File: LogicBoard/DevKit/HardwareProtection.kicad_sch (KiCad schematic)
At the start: 23 parts, among them U11 SN74LVC1G332DCKR, U15 TPL0401B-10DCKR, U16 ATTINY1616-MNR, U17 ATTINY1616-MNR, U2 TPL0401A-10DCKR

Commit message: v2
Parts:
- removed D3: SS14, Diode_SMD:D_SMA, symbol Device:D_Schottky
- removed U2: TPL0401A-10DCKR, Package_TO_SOT_SMD:Texas_R-PDSO-G6, symbol Potentiometer_Digital:TPL0401A-10-Q1
- added D8: 1N5819WS, Diode_SMD:D_SOD-323, symbol Device:D_Schottky
- added D9 (x3): L_FAULT, LED_SMD:LED_0603_1608Metric, symbol Device:LED
- added J4: HWProtDebug, Connector_PinHeader_2.00mm:PinHeader_1x04_P2.00mm_Vertical, symbol Connector_Generic:Conn_01x04
- added R1 (x4): 4.7k, Resistor_SMD:R_0603_1608Metric, symbol Device:R
- added R47 (x3): 10k, Resistor_SMD:R_0603_1608Metric, symbol Device:R
- added U2: TPL0401B-10DCKR, Package_TO_SOT_SMD:Texas_R-PDSO-G6, symbol Potentiometer_Digital:TPL0401B-10-Q1
- C15: footprint Capacitor_SMD:C_0805_2012Metric -> Capacitor_SMD:C_0603_1608Metric; MPN (none) -> C14663
- C23, C24: MPN (none) -> C107145
- C5, C6: footprint Capacitor_SMD:C_0805_2012Metric -> Capacitor_SMD:C_0603_1608Metric; MPN (none) -> C15849
- R15: footprint Resistor_SMD:R_0805_2012Metric -> Resistor_SMD:R_0603_1608Metric; MPN C17414 -> C25804
- R33: footprint Resistor_SMD:R_0805_2012Metric -> Resistor_SMD:R_0603_1608Metric; MPN (none) -> C25804
- R43, R44, R45: footprint Resistor_SMD:R_0805_2012Metric -> Resistor_SMD:R_0603_1608Metric; MPN (none) -> C4190
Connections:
- net +3.3V: now also R1.1, R1.1, R1.1, R1.1, U2.1 (VDD)
- net +3.3VADC: now also U2.6 (H)
- net CURR_TRIP_HIGH: now also U2.5 (W)
- net GND: now also R47.2, R47.2, R47.2, U2.2 (GND)
- net POWER_STAGE_DISABLE: now also D9.2 (A)
- net POWER_STAGE_LOCKOUT: now also D8.1 (K)
- net AT_HIGH_FAULT: now reaches R33.2, U11.6, U16.5 (PA4)
- net AT_HIGH_FAULT: now also D9.2 (A)
- net at U11.4: now also D8.2 (A)
- net AT_LOW_FAULT: now reaches R33.2, U11.1, U17.5 (PA4)
- net AT_LOW_FAULT: now also D9.2 (A)
- net AT_HIGH_RX: now reaches U16.11 (PB3)
- net AT_HIGH_RX: now also J4.3 (Pin_3)
- net AT_HIGH_TX: now reaches U16.12 (PB2)
- net AT_HIGH_TX: now also J4.4 (Pin_4)
- net AT_LOW_SCL: now reaches U17.1 (PA2)
- net AT_LOW_SCL: now also U15.3 (SCL), R1.2
- net AT_LOW_RX: now reaches U17.11 (PB3)
- net AT_LOW_RX: now also J4.1 (Pin_1)
- net AT_LOW_TX: now reaches U17.12 (PB2)
- net AT_LOW_TX: now also J4.2 (Pin_2)
- net AT_LOW_SDA: now reaches U17.20 (PA1)
- net AT_LOW_SDA: now also U15.4 (SDA), R1.2
- net SCL renamed AT_HIGH_SCL
- net AT_HIGH_SCL: now also R1.2, U2.3 (SCL); no longer U15.3 (SCL)
- net SDA renamed AT_HIGH_SDA
- net AT_HIGH_SDA: now also R1.2, U2.4 (SDA); no longer U15.4 (SDA)
- new net: D9.1 (K), R47.1 (x3)
- no-connect marks 18 -> 12
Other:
- note added: "use TPL0401A-10DCKR if B is not available B is cheaper"
- moved on the sheet: C5, C53, C54, C6, R15, U15

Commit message: v2
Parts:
- added TP3: HighTrip, TestPoint:TestPoint_Pad_D1.0mm, symbol Connector:TestPoint
- added TP3: LowTrip, TestPoint:TestPoint_Pad_D1.0mm, symbol Connector:TestPoint
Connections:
- net CLEAR_HW_FAULT: now also U16.9 (PB5), U17.9 (PB5)
- net CURR_TRIP_HIGH: now also TP3.1
- net CURR_TRIP_LOW: now also TP3.1
- no-connect marks 12 -> 10
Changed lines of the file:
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@@
   )
   (no_connect (at 130.81 72.39))
-  (no_connect (at 130.81 100.33))
   (no_connect (at 100.33 172.72))
-  (no_connect (at 130.81 177.8))
   (no_connect (at 100.33 87.63))
   (no_connect (at 100.33 92.71))
@@
     (stroke (width 0) (type default))
   )
-  (wire (pts (xy 67.31 82.55) (xy 54.61 82.55))
+  (wire (pts (xy 64.77 82.55) (xy 54.61 82.55))
     (stroke (width 0) (type default))
   )
@@
     (stroke (width 0) (type default))
   )
-  (wire (pts (xy 67.31 73.66) (xy 67.31 82.55))
+  (wire (pts (xy 64.77 73.66) (xy 64.77 82.55))
     (stroke (width 0) (type default))
   )
@@
     )
   )
+  (global_label "CLEAR_HW_FAULT" (shape input) (at 130.81 100.33 0) (fields_autoplaced)
+    (effects (font (size 1.27 1.27)) (justify left))
+    (property "Intersheetrefs" "${INTERSHEET_REFS}" (at 149.0878 100.33 0)
+      (effects (font (size 1.27 1.27)) (justify left) hide)
+    )
+  )
   (global_label "POWER_STAGE_DISABLE" (shape input) (at 194.31 151.13 180) (fields_autoplaced)
     (effects (font (size 1.27 1.27)) (justify right))
@@
     (effects (font (size 1.27 1.27)) (justify left))
     (property "Intersheetrefs" "${INTERSHEET_REFS}" (at 149.4397 82.55 0)
+      (effects (font (size 1.27 1.27)) (justify left) hide)
+    )
+  )
+  (global_label "CLEAR_HW_FAULT" (shape input) (at 130.81 177.8 0) (fields_autoplaced)
+    (effects (font (size 1.27 1.27)) (justify left))
+    (property "Intersheetrefs" "${INTERSHEET_REFS}" (at 149.0878 177.8 0)
       (effects (font (size 1.27 1.27)) (justify left) hide)
     )
@@
     )
   )
-  (symbol (lib_id "power:+3.3VADC") (at 67.31 73.66 0) (unit 1)
-    (in_bom yes) (on_board yes) (dnp no) (fields_autoplaced)
-    (property "Reference" "#PWR0127" (at 71.12 74.93 0)
-      (effects (font (size 1.27 1.27)) hide)
-    )
-    (property "Value" "+3.3VADC" (at 67.31 68.58 0)
-      (effects (font (size 1.27 1.27)))
-    )
-    (property "Footprint" "" (at 67.31 73.66 0)
-      (effects (font (size 1.27 1.27)) hide)
-    )
-    (property "Datasheet" "" (at 67.31 73.66 0)
+  (symbol (lib_id "power:+3.3VADC") (at 64.77 73.66 0) (unit 1)
+    (in_bom yes) (on_board yes) (dnp no) (fields_autoplaced)
+    (property "Reference" "#PWR0127" (at 68.58 74.93 0)
+      (effects (font (size 1.27 1.27)) hide)
+    )
+    (property "Value" "+3.3VADC" (at 64.77 68.58 0)
+      (effects (font (size 1.27 1.27)))
+    )
+    (property "Footprint" "" (at 64.77 73.66 0)
+      (effects (font (size 1.27 1.27)) hide)
+    )
+    (property "Datasheet" "" (at 64.77 73.66 0)
       (effects (font (size 1.27 1.27)) hide)
     )
@@
     )
   )
+  (symbol (lib_id "Connector:TestPoint") (at 69.85 90.17 0) (unit 1)
+    (in_bom yes) (on_board yes) (dnp no)
+    (property "Reference" "TP3" (at 68.58 81.28 0)
+      (effects (font (size 1.27 1.27)) (justify left))
+    )
+    (property "Value" "HighTrip" (at 66.04 83.82 0)
+      (effects (font (size 1.27 1.27)) (justify left))
+    )
+    (property "Footprint" "TestPoint:TestPoint_Pad_D1.0mm" (at 74.93 90.17 0)
+      (effects (font (size 1.27 1.27)) hide)
+    )
+    (property "Datasheet" "~" (at 74.93 90.17 0)
+      (effects (font (size 1.27 1.27)) hide)
+    )
+    (pin "1")
+    (instances
+      (project "DevKit"
+        (path "/768a484b-8a27-40cf-8cad-0f63935b1af0"
+          (reference "TP3") (unit 1)
+        )
+        (path "/768a484b-8a27-40cf-8cad-0f63935b1af0/81081265-f675-4f9d-bffe-8ec1eaaaba23"
+          (reference "TP3") (unit 1)
+        )
+      )
+    )
+  )
   (symbol (lib_id "Device:R") (at 200.66 34.29 0) (unit 1)
     (in_bom yes) (on_board yes) (dnp no) (fields_autoplaced)
@@
         )
       )
+    )
+  )
+  (symbol (lib_id "Connector:TestPoint") (at 71.12 161.29 0) (unit 1)
+    (in_bom yes) (on_board yes) (dnp no)
+    (property "Reference" "TP3" (at 69.85 152.4 0)
+      (effects (font (size 1.27 1.27)) (justify left))
+    )
+    (property "Value" "LowTrip" (at 67.31 154.94 0)
+      (effects (font (size 1.27 1.27)) (justify left))
+    )
+    (property "Footprint" "TestPoint:TestPoint_Pad_D1.0mm" (at 76.2 161.29 0)
+      (effects (font (size 1.27 1.27)) hide)
+    )
+    (property "Datasheet" "~" (at 76.2 161.29 0)
+      (effects (font (size 1.27 1.27)) hide)
+    )
+    (pin "1")
+    (instances
+      (project "DevKit"
+        (path "/768a484b-8a27-40cf-8cad-0f63935b1af0"
+          (reference "TP3") (unit 1)
+        )
+        (path "/768a484b-8a27-40cf-8cad-0f63935b1af0/81081265-f675-4f9d-bffe-8ec1eaaaba23"
+          (reference "TP4") (unit 1)
+        )
+      )

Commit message: initialv2
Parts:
- removed C5, C6: 1u, Capacitor_SMD:C_0603_1608Metric, symbol Device:C
- removed C53, C54, C55, C56: 1u, Capacitor_SMD:C_0402_1005Metric, symbol Device:C
- removed D9 (x2): L_FAULT, LED_SMD:LED_0603_1608Metric, symbol Device:LED
- removed J4: HWProtDebug, Connector_PinHeader_2.00mm:PinHeader_1x04_P2.00mm_Vertical, symbol Connector_Generic:Conn_01x04
- removed R1 (x4): 4.7k, Resistor_SMD:R_0603_1608Metric, symbol Device:R
- removed R47 (x2): 10k, Resistor_SMD:R_0603_1608Metric, symbol Device:R
- removed TP3: HighTrip, TestPoint:TestPoint_Pad_D1.0mm, symbol Connector:TestPoint
- removed TP3: LowTrip, TestPoint:TestPoint_Pad_D1.0mm, symbol Connector:TestPoint
- removed U15, U2: TPL0401B-10DCKR, Package_TO_SOT_SMD:Texas_R-PDSO-G6, symbol Potentiometer_Digital:TPL0401B-10-Q1
- removed U16, U17: ATTINY1616-MNR, Package_DFN_QFN:VQFN-20-1EP_3x3mm_P0.4mm_EP1.7x1.7mm, symbol MCU_Microchip_ATtiny:ATtiny1616-M
- C22, C23, C24: value 220p 50v -> 220p; footprint Capacitor_SMD:C_0805_2012Metric -> Capacitor_SMD:C_0603_1608Metric; MPN C107145 -> C1603
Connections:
- net AT_HIGH_FAULT renamed ComparatorHigh/LATCH_OUT
- net AT_LOW_FAULT renamed ComparatorLow/LATCH_OUT
- no-connect marks 10 -> 0
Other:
- added sheet ComparatorHigh (ATTinyComp.kicad_sch)
- added sheet ComparatorLow (ATTinyComp.kicad_sch)
- note added: "330kHz Filters"
- note removed: "use TPL0401A-10DCKR if B is not available B is cheaper"
- moved on the sheet: D9, R15, R47

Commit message: v2
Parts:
- removed C22, C23, C24: 220p, Capacitor_SMD:C_0603_1608Metric, symbol Device:C
- removed R43, R44, R45: 2.2k, Resistor_SMD:R_0603_1608Metric, symbol Device:R
- C15: footprint Capacitor_SMD:C_0603_1608Metric -> GigaVescLibs:C_0603_1608Metric_L
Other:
- note removed: "330kHz Filters"
- moved on the sheet: D9, R15, R47

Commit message: small fixes
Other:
- note added: "If you do not want to use hardware protection, also remember to not solder R26 and R31"
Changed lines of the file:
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@@
+    (effects (font (size 1.27 1.27)) (justify left bottom))
+  )
+  (text "If you do not want to use hardware protection, also remember to not solder R26 and R31"
+    (at 72.39 35.56 0)
     (effects (font (size 1.27 1.27)) (justify left bottom))
   )

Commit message: v2.7.0 - Phase shunts
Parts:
- added C22, C23, C24: 1n, GigaVescLibs:C_0603_1608Metric_L, symbol Device:C
- added R43 (x3): 1k, Resistor_SMD:R_0603_1608Metric, symbol Device:R
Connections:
- net CURR1_FILTERED: now also C24.1, R43.1
- net CURR2_FILTERED: now also C23.1, R43.1
- net CURR3_FILTERED: now also C22.2, R43.1
- net GND: now also C22.1, C23.2, C24.2
- new net CURR1: R43.2
- new net CURR2: R43.2
- new net CURR3: R43.2

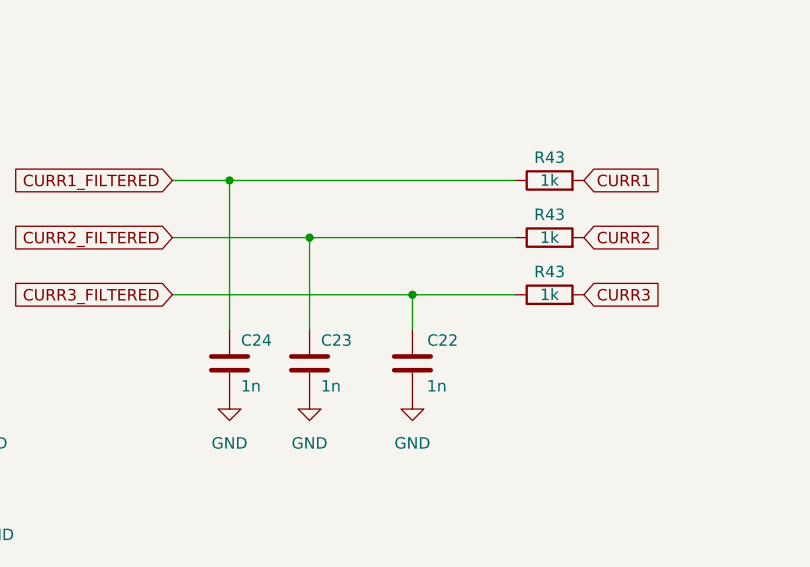
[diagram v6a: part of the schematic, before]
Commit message: v2.10.0 - Low side shunt and hall sensor - current filters
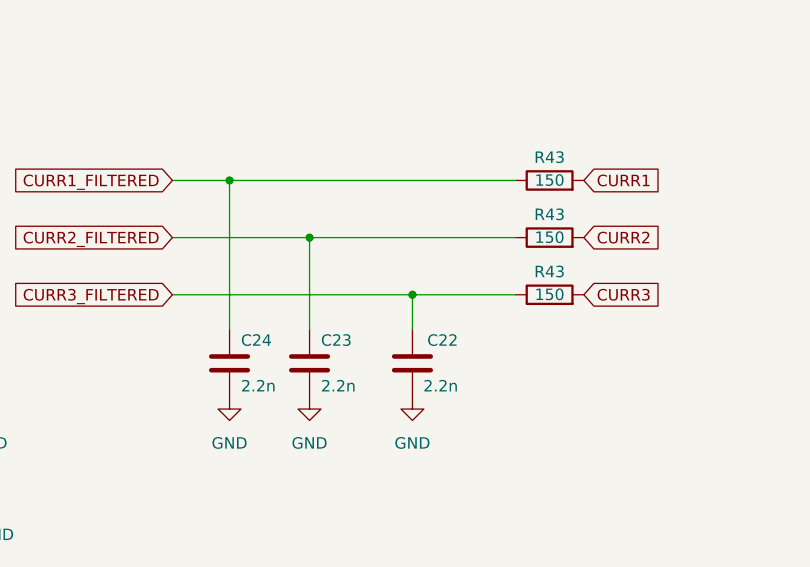
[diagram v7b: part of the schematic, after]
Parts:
- C22, C23, C24: value 1n -> 2.2n; MPN C1588 -> C1604
- R43: value 1k -> 150; MPN C21190 -> C22808
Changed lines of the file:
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@@
       (effects (font (size 1.27 1.27)))
     )
-    (property "Value" "1k" (at 229.87 93.98 90)
+    (property "Value" "150" (at 229.87 93.98 90)
       (effects (font (size 1.27 1.27)))
     )
@@
       (effects (font (size 1.27 1.27)) hide)
     )
-    (property "MPN" "C21190" (at 229.87 93.98 0)
+    (property "MPN" "C22808" (at 229.87 93.98 0)
       (effects (font (size 1.27 1.27)) hide)
     )
@@
       (effects (font (size 1.27 1.27)) (justify left))
     )
-    (property "Value" "1n" (at 218.44 110.49 0)
+    (property "Value" "2.2n" (at 219.71 110.49 0)
       (effects (font (size 1.27 1.27)) (justify left))
     )
@@
       (effects (font (size 1.27 1.27)) hide)
     )
-    (property "MPN" "C1588" (at 214.63 107.95 0)
+    (property "MPN" "C1604" (at 214.63 107.95 0)
       (effects (font (size 1.27 1.27)) hide)
     )
@@
       (effects (font (size 1.27 1.27)))
     )
-    (property "Value" "1k" (at 229.87 87.63 90)
+    (property "Value" "150" (at 229.87 87.63 90)
       (effects (font (size 1.27 1.27)))
     )
@@
       (effects (font (size 1.27 1.27)) hide)
     )
-    (property "MPN" "C21190" (at 229.87 87.63 0)
+    (property "MPN" "C22808" (at 229.87 87.63 0)
       (effects (font (size 1.27 1.27)) hide)
     )
@@
       (effects (font (size 1.27 1.27)))
     )
-    (property "Value" "1k" (at 229.87 100.33 90)
+    (property "Value" "150" (at 229.87 100.33 90)
       (effects (font (size 1.27 1.27)))
     )
@@
       (effects (font (size 1.27 1.27)) hide)
     )
-    (property "MPN" "C21190" (at 229.87 100.33 0)
+    (property "MPN" "C22808" (at 229.87 100.33 0)
       (effects (font (size 1.27 1.27)) hide)
     )
@@
       (effects (font (size 1.27 1.27)) (justify left))
     )
-    (property "Value" "1n" (at 195.58 110.49 0)
+    (property "Value" "2.2n" (at 195.58 110.49 0)
       (effects (font (size 1.27 1.27)) (justify left))
     )
@@
       (effects (font (size 1.27 1.27)) hide)
     )
-    (property "MPN" "C1588" (at 194.31 107.95 0)
+    (property "MPN" "C1604" (at 194.31 107.95 0)
       (effects (font (size 1.27 1.27)) hide)
     )
@@
       (effects (font (size 1.27 1.27)) (justify left))
     )
-    (property "Value" "1n" (at 204.47 110.49 0)
+    (property "Value" "2.2n" (at 204.47 110.49 0)
       (effects (font (size 1.27 1.27)) (justify left))
     )
@@
       (effects (font (size 1.27 1.27)) hide)
     )
-    (property "MPN" "C1588" (at 203.2 107.95 0)
-      (effects (font (size 1.27 1.27)) hide)
-    )
+    (property "MPN" "C1604" (at 203.2 107.95 0)
+      (effects (font (size 1.27 1.27)) hide)
+    )

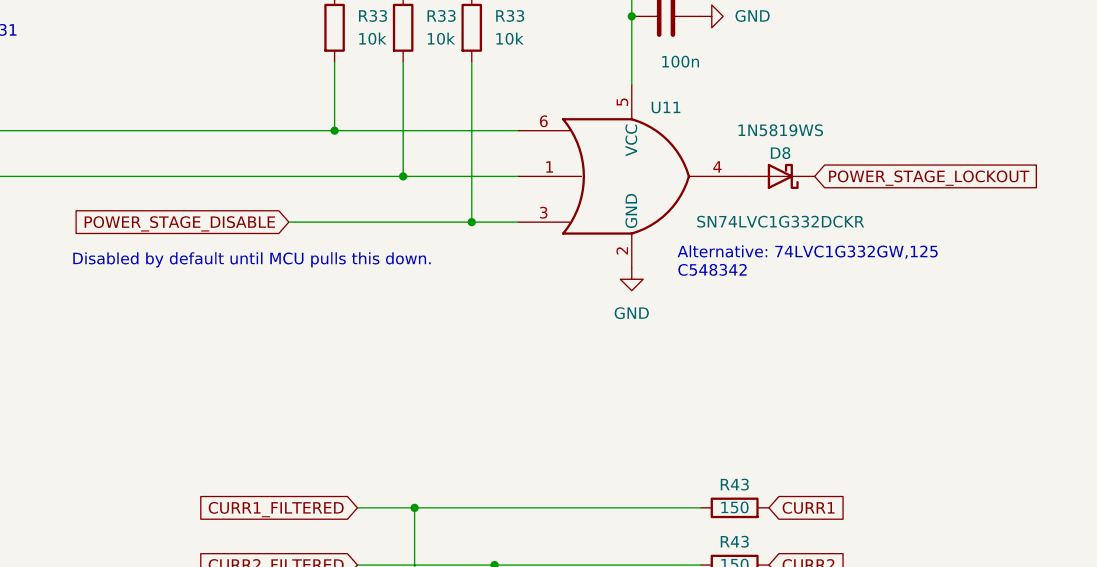
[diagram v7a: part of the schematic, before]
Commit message: v3.0.3 - Cosmetic Changes
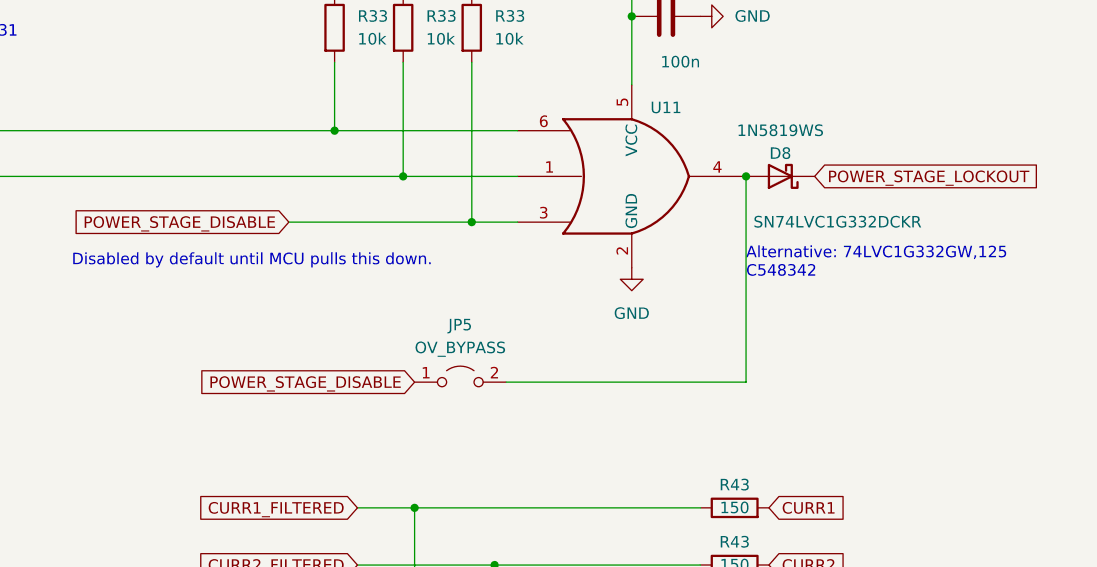
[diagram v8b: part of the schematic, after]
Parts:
- added JP5: OV_BYPASS, Jumper:SolderJumper-2_P1.3mm_Open_TrianglePad1.0x1.5mm, symbol Jumper:Jumper_2_Open
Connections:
- net POWER_STAGE_DISABLE: now also JP5.1 (A)
- net at D8.2 (A), U11.4: now also JP5.2 (B)
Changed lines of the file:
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@@
   (junction (at 95.25 53.34) (diameter 0) (color 0 0 0 0)
   )
+  (junction (at 231.14 50.8) (diameter 0) (color 0 0 0 0)
+  )
   (junction (at 200.66 55.88) (diameter 0) (color 0 0 0 0)
   )
@@
     (stroke (width 0) (type default))
   )
+  (wire (pts (xy 204.47 73.66) (xy 231.14 73.66))
+    (stroke (width 0) (type default))
+  )
   (wire (pts (xy 127 90.17) (xy 127 50.8))
     (stroke (width 0) (type default))
@@
     (stroke (width 0) (type default))
   )
+  (wire (pts (xy 231.14 73.66) (xy 231.14 50.8))
+    (stroke (width 0) (type default))
+  )
   (wire (pts (xy 214.63 104.14) (xy 214.63 100.33))
     (stroke (width 0) (type default))
@@
     (stroke (width 0) (type default))
   )
-  (text "Alternative: 74LVC1G332GW,125\nC548342" (at 223.52 62.23 0)
+  (text "Alternative: 74LVC1G332GW,125\nC548342" (at 231.14 62.23 0)
     (effects (font (size 1.27 1.27)) (justify left bottom))
   )
@@
     )
   )
+  (global_label "POWER_STAGE_DISABLE" (shape input) (at 194.31 73.66 180) (fields_autoplaced)
+    (effects (font (size 1.27 1.27)) (justify right))
+    (property "Intersheetrefs" "${INTERSHEET_REFS}" (at 170.3476 73.66 0)
+      (effects (font (size 1.27 1.27)) (justify right) hide)
+    )
+  )
   (global_label "CURR2" (shape input) (at 233.68 93.98 0) (fields_autoplaced)
     (effects (font (size 1.27 1.27)) (justify left))
@@
       (effects (font (size 1.27 1.27)))
     )
-    (property "Value" "SN74LVC1G332DCKR" (at 234.95 55.88 0)
+    (property "Value" "SN74LVC1G332DCKR" (at 241.3 55.88 0)
       (effects (font (size 1.27 1.27)))
     )
@@
         )
       )
+    )
+  )
+  (symbol (lib_id "Jumper:Jumper_2_Open") (at 199.39 73.66 0) (unit 1)
+    (in_bom no) (on_board yes) (dnp no) (fields_autoplaced)
+    (property "Reference" "JP5" (at 199.39 67.31 0)
+      (effects (font (size 1.27 1.27)))
+    )
+    (property "Value" "OV_BYPASS" (at 199.39 69.85 0)
+      (effects (font (size 1.27 1.27)))
+    )
+    (property "Footprint" "Jumper:SolderJumper-2_P1.3mm_Open_TrianglePad1.0x1.5mm" (at 199.39 73.66 0)
+      (effects (font (size 1.27 1.27)) hide)
+    )
+    (property "Datasheet" "~" (at 199.39 73.66 0)
+      (effects (font (size 1.27 1.27)) hide)
+    )
+    (pin "1")
+    (pin "2")
+    (instances
+      (project "DevKit"
+        (path "/768a484b-8a27-40cf-8cad-0f63935b1af0/81081265-f675-4f9d-bffe-8ec1eaaaba23"
+          (reference "JP5") (unit 1)
+        )
+      )
